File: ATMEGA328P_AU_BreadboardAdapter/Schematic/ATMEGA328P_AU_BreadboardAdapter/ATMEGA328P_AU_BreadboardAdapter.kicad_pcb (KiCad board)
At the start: 2 copper layers, 38.2 x 21.2 mm, 23 parts, among them J1 FTDI, J2 Pin header 1, J3 Pin header 2, SW1 RESET, U1 AMS1117-5.0, U2 ATMEGA328P-AU, Y1 16MHz

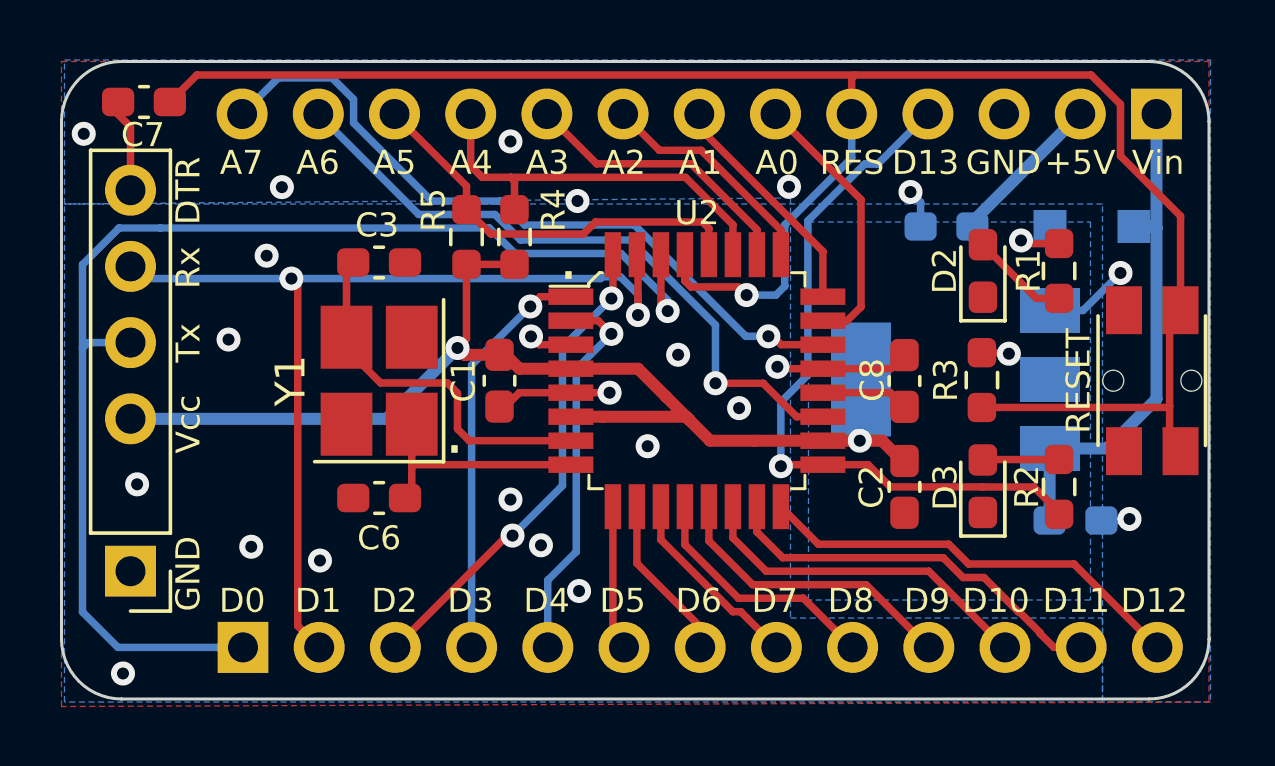
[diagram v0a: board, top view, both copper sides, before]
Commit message: LDO replaced by buck regulator
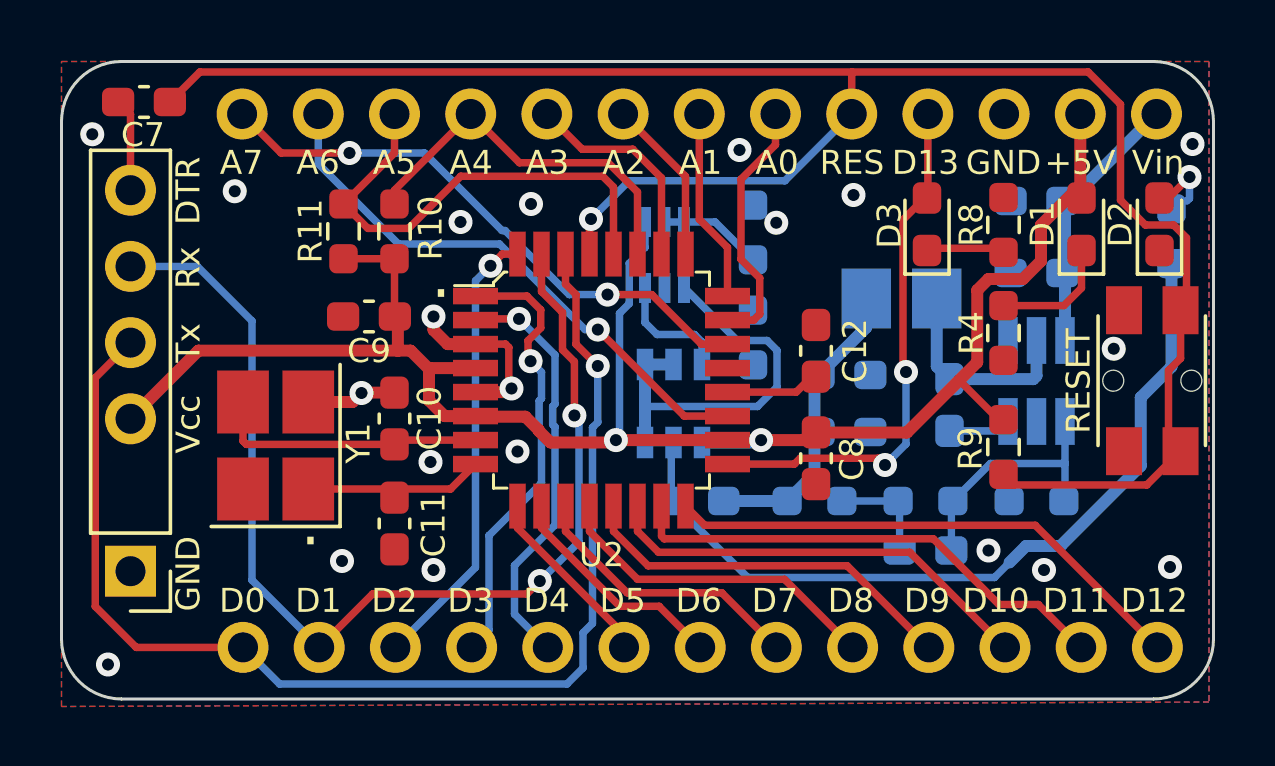
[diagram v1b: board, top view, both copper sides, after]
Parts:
- added C1: 100nF, Capacitor_SMD:C_0603_1608Metric_Pad1.08x0.95mm_HandSolder, B.Cu at (187.1, 82.7)
- added C2: 22µF 10V, Capacitor_SMD:C_0603_1608Metric_Pad1.08x0.95mm_HandSolder, B.Cu at (183.6, 83.6)
- added C3: 22µF 10V, Capacitor_SMD:C_0603_1608Metric_Pad1.08x0.95mm_HandSolder, B.Cu at (183.6, 81.7)
- added C6: 75pF, Capacitor_SMD:C_0603_1608Metric_Pad1.08x0.95mm_HandSolder, B.Cu at (186.3, 87.5)
- added FB1: FerriteBead_Small, Inductor_SMD:L_0603_1608Metric_Pad1.05x0.95mm_HandSolder, B.Cu at (178.7, 85.9)
- added G***: LOGO, Graphics:retronics_logo_14mm, B.Cu at (162.3, 81.9)
- added L1: 10µH 1A, Inductor_SMD:L_Taiyo-Yuden_NR-20xx_HandSoldering, B.Cu at (185.5, 79.2)
- added Q1: Si3493DDV, SamacSys_Parts:SOT95P280X100-6N, B.Cu at (177.9, 82.7)
- added Q2: BC857BS, myDevices:SOT-363_SC-70-6-Handsoldering, B.Cu at (177.6, 77.7)
- added R2: 560Ω, Resistor_SMD:R_0603_1608Metric_Pad0.98x0.95mm_HandSolder, B.Cu at (194.5, 77.1)
- added R3: 100kΩ, Resistor_SMD:R_0603_1608Metric_Pad0.98x0.95mm_HandSolder, B.Cu at (186.3, 85.9)
- added R4: 560Ω, Resistor_SMD:R_0603_1608Metric_Pad0.98x0.95mm_HandSolder, F.Cu at (188.9, 80.3)
- added R5: 13.3kΩ, Resistor_SMD:R_0603_1608Metric_Pad0.98x0.95mm_HandSolder, B.Cu at (190.0, 85.9)
- added R6: 10kΩ, Resistor_SMD:R_0603_1608Metric_Pad0.98x0.95mm_HandSolder, B.Cu at (180.6, 77.0)
- added R7: 10kΩ, Resistor_SMD:R_0603_1608Metric_Pad0.98x0.95mm_HandSolder, B.Cu at (180.6, 80.5)
- C4: value 10µF -> 10µF 35V
- C5: value 10µF -> 100nF
- D1: value 1N5819W -> "Vcc"; footprint Diode_SMD:D_SOD-123F -> LED_SMD:LED_0603_1608Metric_Pad1.05x0.95mm_HandSolder; moved to F.Cu
- D2: value Green -> "Vin"
- D3: value Blue -> "D13"
- R1: value 560Ω -> 49.9Ω; moved to B.Cu
- U1: value AMS1117-5.0 -> TPS54302; footprint Package_TO_SOT_SMD:SOT-223-3_TabPin2 -> Package_TO_SOT_SMD:SOT-23-6_Handsoldering
- moved C9 18.7 mm to (167.8, 79.8), turned to 0 degrees
- moved R1 11.2 mm to (182.6, 85.9), turned to 0 degrees
- moved C8 10.9 mm to (182.7, 84.5)
- moved C4 10.7 mm to (190.0, 75.9), turned to 0 degrees
- moved D3 8.93 mm to (186.3, 76.7)
- moved R8 8.93 mm to (188.9, 76.7)
- moved D2 6.09 mm to (194.1, 76.7)
- moved C10 5.23 mm to (168.6, 83.2), turned to 90 degrees
- moved R11 4.10 mm to (166.9, 76.9)
- moved Y1 4.07 mm to (164.6, 84.0)
- moved R10 4.00 mm to (168.6, 76.9)
- moved C5 3.38 mm to (190.0, 78.3)
- moved U2 3.18 mm to (175.5, 81.9)
- moved C12 3.12 mm to (182.7, 80.9)
- moved U1 2.70 mm to (190.0, 81.9), turned to -90 degrees
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- renumbered C3 to C10, C6 to C11, C8 to C12, C1 to C8, C2 to C9, J2 to J1, J3 to J2, J1 to J3, R4 to R10, R5 to R11, R2 to R8, R3 to R9
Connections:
- C4 pad 2: VCC -> VDC
- C5 pad 2: +5V -> VDC
- C8 pad 2: +5V -> VCC
- C9 pad 2: +5V -> VCC
- D1 pad 1: VCC -> Net-(D1-Pad1)
- D1 pad 2: +5V -> VCC
- D2 pad 2: Net-(D2-Pad2) -> Net-(R2-Pad2)
- D3 pad 1: GND -> Net-(D3-Pad1)
- D3 pad 2: Net-(D3-Pad2) -> D13
- J2 pad 1: VCC -> VDC
- J2 pad 2: +5V -> VCC
- J3 pad 3: +5V -> VCC
- R1 pad 1: +5V -> Net-(C2-Pad2)
- R1 pad 2: Net-(D2-Pad2) -> Net-(C6-Pad2)
- R10 pad 2: +5V -> VCC
- R11 pad 1: +5V -> VCC
- R8 pad 1: Net-(D3-Pad2) -> GND
- R8 pad 2: D13 -> Net-(D3-Pad1)
- R9 pad 1: +5V -> VCC
- U1 pad 2: +5V -> Net-(C1-Pad1)
- U1 pad 3: VCC -> VDC
- U2 pad 18: +5V -> VCC
- U2 pad 4: +5V -> VCC
- U2 pad 6: +5V -> VCC
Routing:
- net +5V: track 44.2 -> 0.00 mm, vias 4 -> 0
- net VCC: track 16.9 -> 60.5 mm, vias 0 -> 2
- net Net-(FB1-Pad2): track 0.00 -> 41.8 mm
- net Net-(C2-Pad2): track 0.00 -> 9.95 mm
- net VDC: track 0.00 -> 9.02 mm
- net Net-(C6-Pad1): track 0.00 -> 8.59 mm
- net Net-(C1-Pad1): track 0.00 -> 6.99 mm
- net D13: track 24.1 -> 17.8 mm, vias 1 -> 2
- net GND: track 14.7 -> 8.86 mm, vias 23 -> 20
- net Net-(Q2-Pad2): track 0.00 -> 5.67 mm
- net Net-(Q1-Pad3): track 0.00 -> 5.53 mm
- net A7: track 23.6 -> 19.4 mm, vias 1 -> 2
- net Net-(D1-Pad1): track 0.00 -> 4.17 mm
- net D1: track 32.7 -> 36.8 mm
- net Net-(C6-Pad2): track 0.00 -> 3.55 mm
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- removed copper zone on B.Cu, net +5V
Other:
- board size 38.2 x 21.2 mm -> 38.4 x 21.2 mm
- board text added: "8MHz-3.3V 16MHz-5V"
- board text added: "ATMEGA328P-AU Basic R0129A_2309_Pb Bjørner Sandom"
- board text added: "JLCJLCJLCJLC"
- board text removed: "ATMEGA328P-AU Basic R0129-2309 Bjørner Sandom retronics.no"
